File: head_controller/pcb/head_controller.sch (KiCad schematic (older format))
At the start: 64 parts, among them P1 PWR_JACK_2.5x5.5, P2 HEADER_01X03, P3 BNC_DOUBLE_RA, P4 HEADER_02X08_SMD, P5 HEADER_02X08_SMD, P6 HEADER_02X08_SMD, P7 HEADER_02X08_SMD, SW1 SPST_SERIES_M, SW2 KT_SWITCH, U1 MAX6817, U2 MAX6817, U3 TLE723X, U4 TLE723X, U5 TLE723X, U6 TLE723X

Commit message: Added footprints.
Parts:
- removed ARDUINO1: ARDUINO_MEGA, head_controller:ARDUINO_MEGA_SHIELD, symbol ARDUINO_MEGA
- removed C7, C8, C9: 0.1uF, head_controller:SM1210, symbol 0.1uF
- removed D10, D11, D12, D18, D19, D2, D20, D21, D22, D23, D24, D25, D26, D27, D28, D3, D4, D5, D6, D7, D8, D9: LED_24V, head_controller:LED_555-3XXX, symbol LED_24V
- removed P5, P6, P7: HEADER_02X08_SMD, head_controller:HEADER_02x08_SMD, symbol HEADER_02X08_SMD
- removed R3: 5.11k, head_controller:SM1210, symbol 5.11k
- removed SW1: SPST_SERIES_M, head_controller:SPST_SERIES_M, symbol SPST_SERIES_M
- removed U3, U4, U5, U6: TLE723X, head_controller:TLE723X, symbol TLE723X
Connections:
- net labels removed: OUT10, OUT16, OUT17, OUT18, OUT19, OUT20, OUT21, OUT22, OUT23, OUT24, OUT25, OUT26, OUT8, OUT9, RST, SI1, SI2, SI3
- wire segments 346 -> 143
- no-connect marks 65 -> 27

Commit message: Added valve controls to schematic.
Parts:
- removed C1, C2, C3: 10uF, head_controller:SM1210, symbol 10uF
- removed C4, C5, C6: 0.1uF, head_controller:SM1210, symbol 0.1uF
- removed D1, D13, D14, D15, D16, D17, D29, D30, D31, D32, D33: LED_24V, head_controller:LED_555-3XXX, symbol LED_24V
- removed E1: ENCODER_C14, head_controller:Micro-MaTch_6_SMD, symbol ENCODER_C14
- removed P1: PWR_JACK_2.5x5.5, head_controller:DCJACK_2PIN_HIGHCURRENT, symbol PWR_JACK_2.5x5.5
- removed P2: HEADER_01X03, footprints:Header_3_Pin, symbol HEADER_01X03
- removed P3: BNC_DOUBLE_RA, head_controller:BNC_DOUBLE, symbol BNC_DOUBLE_RA
- removed R1, R2: 5.11k, head_controller:SM1210, symbol 5.11k
- removed REG1: CONV_DC_DC_12V_1A, head_controller:DC_DC_CONV_R78C, symbol CONV_DC_DC_12V_1A
- removed S1: HEADER_01X02_SHR, head_controller:Header_Shrouded_2_Pin, symbol HEADER_01X02_SHR
- removed SW2: KT_SWITCH, head_controller:KT_SWITCH, symbol KT_SWITCH
- removed U1, U2: MAX6817, head_controller:MAX6817, symbol MAX6817
- added D1, D2, D3, D4, D5, D6, D7: LED_24V_SMD, head_controller:LED_555-3XXX_SMD, symbol LED_24V_SMD
- added S1, S2, S3, S4, S5, S6, S7: HEADER_01X02_SMD, header_controller:Header_2_Pin_SMD, symbol HEADER_01X02_SMD
- renumbered P4 to P1
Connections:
- net labels removed: +5V, +5VD, BNC_A, BNC_B, BTN, CS, D_BTN, D_ENC_BTN, D_LED_PWR, D_SWITCH, ENC_A, ENC_B, ENC_BTN, GND, IN, LED_PWR, MISO, MOSI, OUT11, OUT12, OUT13, OUT14, OUT15, OUT27, OUT28, OUT29, OUT30, OUT31, OUT7, SCK, SWITCH, TX3, V_IN
- wire segments 143 -> 47
- no-connect marks 27 -> 1
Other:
- moved on the sheet: P1

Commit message: Fixed typos.
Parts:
- S1, S2, S3, S4, S5, S6, S7: footprint header_controller:Header_2_Pin_SMD -> head_controller:Header_2_Pin_SMD
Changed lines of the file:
@@
 F 0 "S1" H 1700 2600 50  0000 C CNN
 F 1 "HEADER_01X02_SMD" V 1800 2450 50  0000 C CNN
-F 2 "header_controller:Header_2_Pin_SMD" H 1600 2500 60  0001 C CNN
+F 2 "head_controller:Header_2_Pin_SMD" H 1600 2500 60  0001 C CNN
 F 3 "" H 1700 2450 60  0000 C CNN
 F 4 "digikey" H 1800 2700 60  0001 C CNN "Vendor"
@@
 F 0 "S2" H 1700 3400 50  0000 C CNN
 F 1 "HEADER_01X02_SMD" V 1800 3250 50  0000 C CNN
-F 2 "header_controller:Header_2_Pin_SMD" H 1600 3300 60  0001 C CNN
+F 2 "head_controller:Header_2_Pin_SMD" H 1600 3300 60  0001 C CNN
 F 3 "" H 1700 3250 60  0000 C CNN
 F 4 "digikey" H 1800 3500 60  0001 C CNN "Vendor"
@@
 F 0 "S3" H 1700 4200 50  0000 C CNN
 F 1 "HEADER_01X02_SMD" V 1800 4050 50  0000 C CNN
-F 2 "header_controller:Header_2_Pin_SMD" H 1600 4100 60  0001 C CNN
+F 2 "head_controller:Header_2_Pin_SMD" H 1600 4100 60  0001 C CNN
 F 3 "" H 1700 4050 60  0000 C CNN
 F 4 "digikey" H 1800 4300 60  0001 C CNN "Vendor"
@@
 F 0 "S4" H 1700 5000 50  0000 C CNN
 F 1 "HEADER_01X02_SMD" V 1800 4850 50  0000 C CNN
-F 2 "header_controller:Header_2_Pin_SMD" H 1600 4900 60  0001 C CNN
+F 2 "head_controller:Header_2_Pin_SMD" H 1600 4900 60  0001 C CNN
 F 3 "" H 1700 4850 60  0000 C CNN
 F 4 "digikey" H 1800 5100 60  0001 C CNN "Vendor"
@@
 F 0 "S5" H 1700 5800 50  0000 C CNN
 F 1 "HEADER_01X02_SMD" V 1800 5650 50  0000 C CNN
-F 2 "header_controller:Header_2_Pin_SMD" H 1600 5700 60  0001 C CNN
+F 2 "head_controller:Header_2_Pin_SMD" H 1600 5700 60  0001 C CNN
 F 3 "" H 1700 5650 60  0000 C CNN
 F 4 "digikey" H 1800 5900 60  0001 C CNN "Vendor"
@@
 F 0 "S6" H 1700 6600 50  0000 C CNN
 F 1 "HEADER_01X02_SMD" V 1800 6450 50  0000 C CNN
-F 2 "header_controller:Header_2_Pin_SMD" H 1600 6500 60  0001 C CNN
+F 2 "head_controller:Header_2_Pin_SMD" H 1600 6500 60  0001 C CNN
 F 3 "" H 1700 6450 60  0000 C CNN
 F 4 "digikey" H 1800 6700 60  0001 C CNN "Vendor"
@@
 F 0 "S7" H 1700 7400 50  0000 C CNN
 F 1 "HEADER_01X02_SMD" V 1800 7250 50  0000 C CNN
-F 2 "header_controller:Header_2_Pin_SMD" H 1600 7300 60  0001 C CNN
+F 2 "head_controller:Header_2_Pin_SMD" H 1600 7300 60  0001 C CNN
 F 3 "" H 1700 7250 60  0000 C CNN
 F 4 "digikey" H 1800 7500 60  0001 C CNN "Vendor"

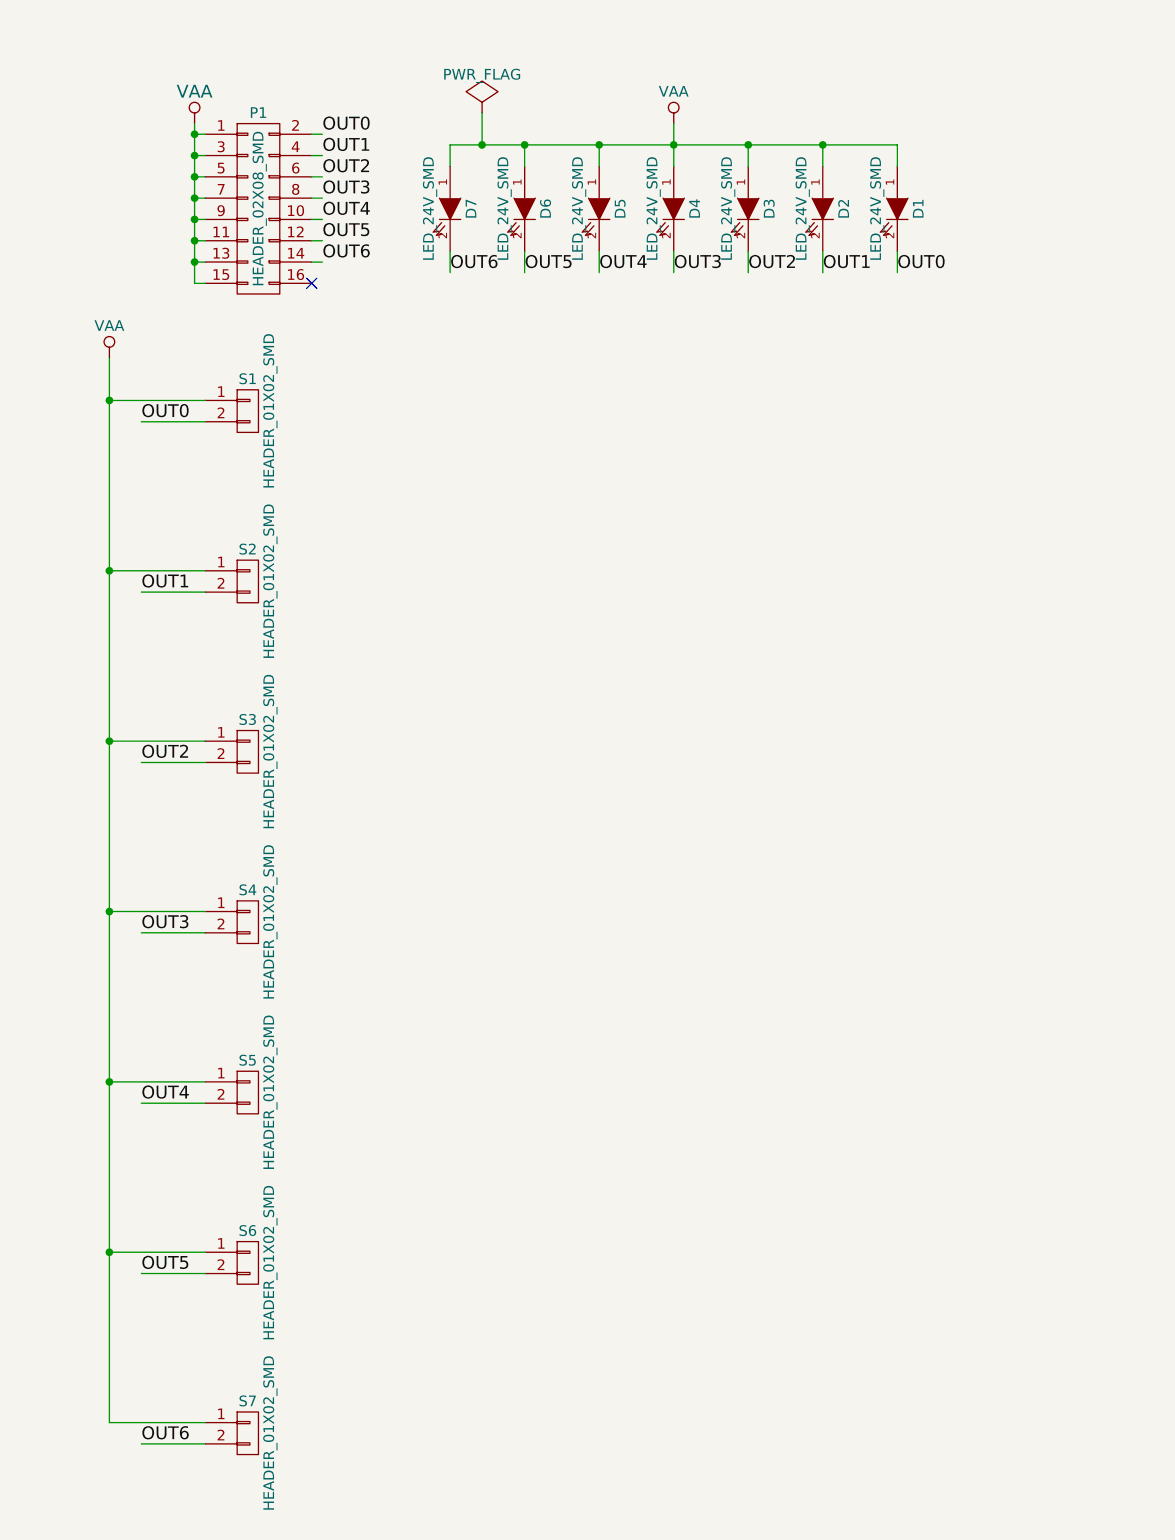
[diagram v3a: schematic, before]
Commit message: Expanded board and added 8th valve and led.
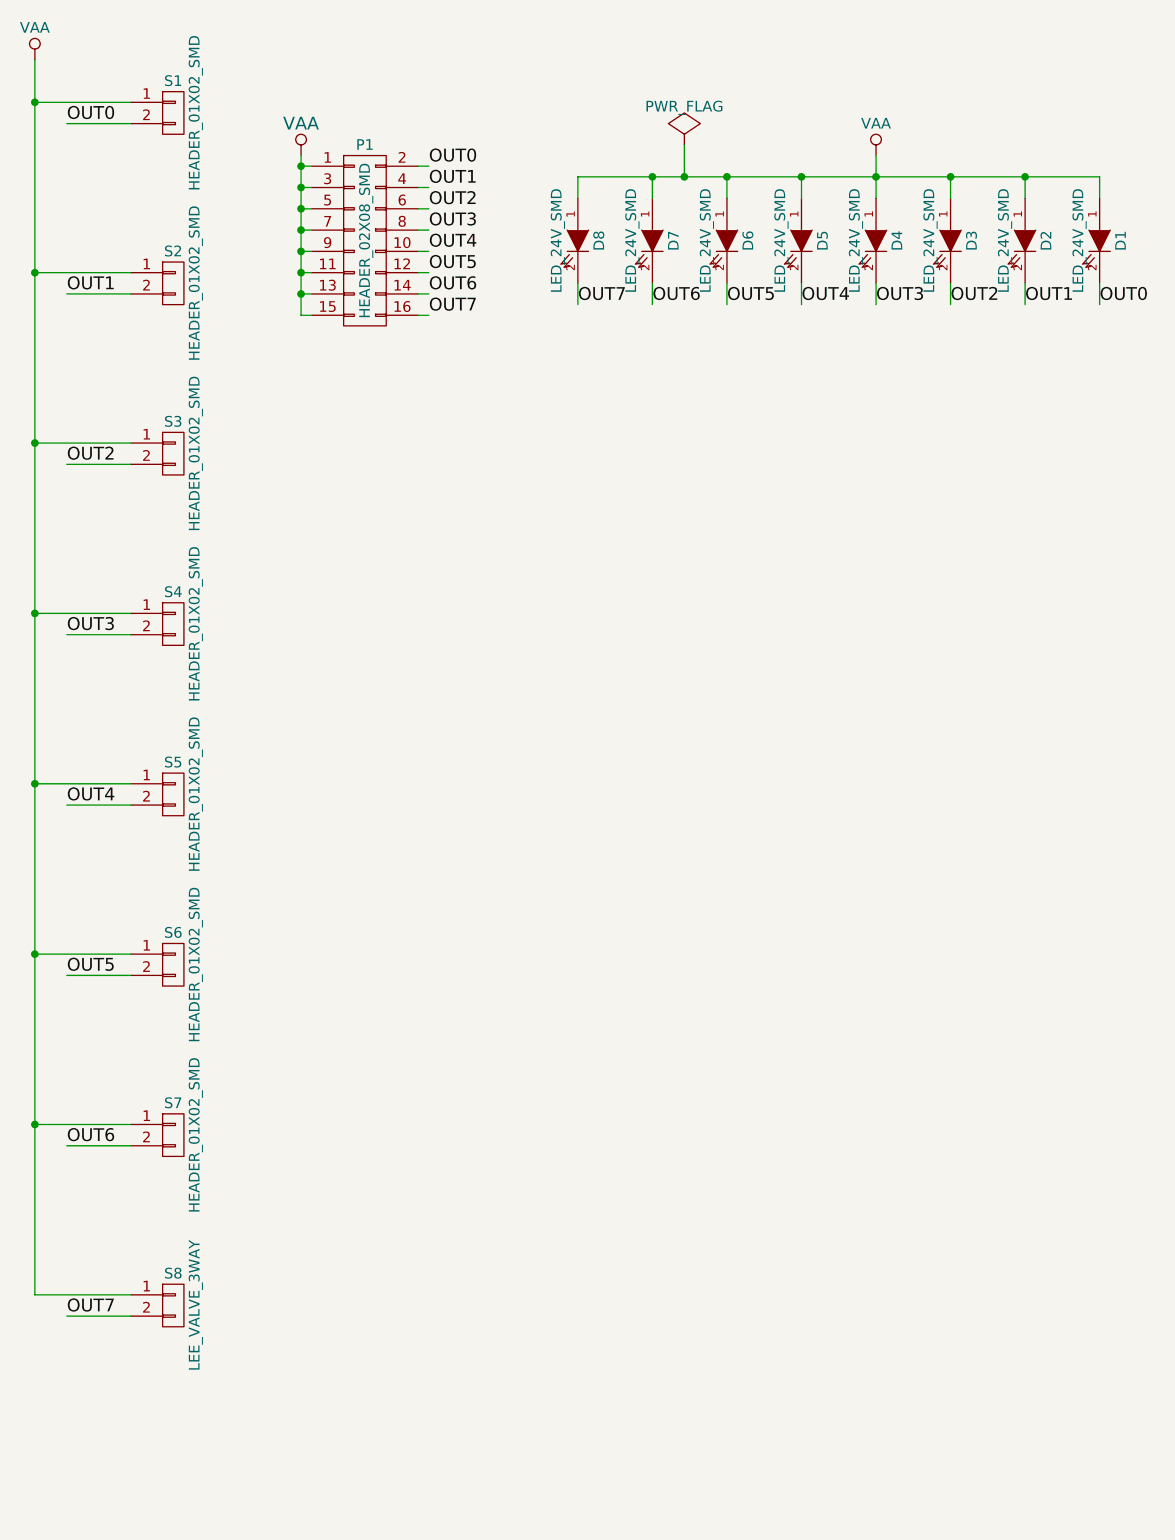
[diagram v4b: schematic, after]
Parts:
- added D8: LED_24V_SMD, head_controller:LED_555-3XXX_SMD, symbol LED_24V_SMD
- added S8: LEE_VALVE_3WAY, head_controller:LEE_VALVE_PLUG_IN, symbol LEE_VALVE_3WAY
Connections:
- net VAA: now also D8.1 (A), S8.1 (P1)
- net OUT7: now reaches P1.16 (P16)
- net OUT7: now also D8.2 (K), S8.2 (P2)
- no-connect marks 1 -> 0
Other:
- moved on the sheet: D1, D2, D3, D4, D5, D6, D7, P1, S1, S2, S3, S4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
